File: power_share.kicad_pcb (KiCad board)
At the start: 2 copper layers, 32.5 x 21.1 mm, 22 parts, among them J1 Conn_01x02, J2 Conn_01x03, Q1 NX3008NBKW, Q2 NX3008NBKW, U1 LTC4370

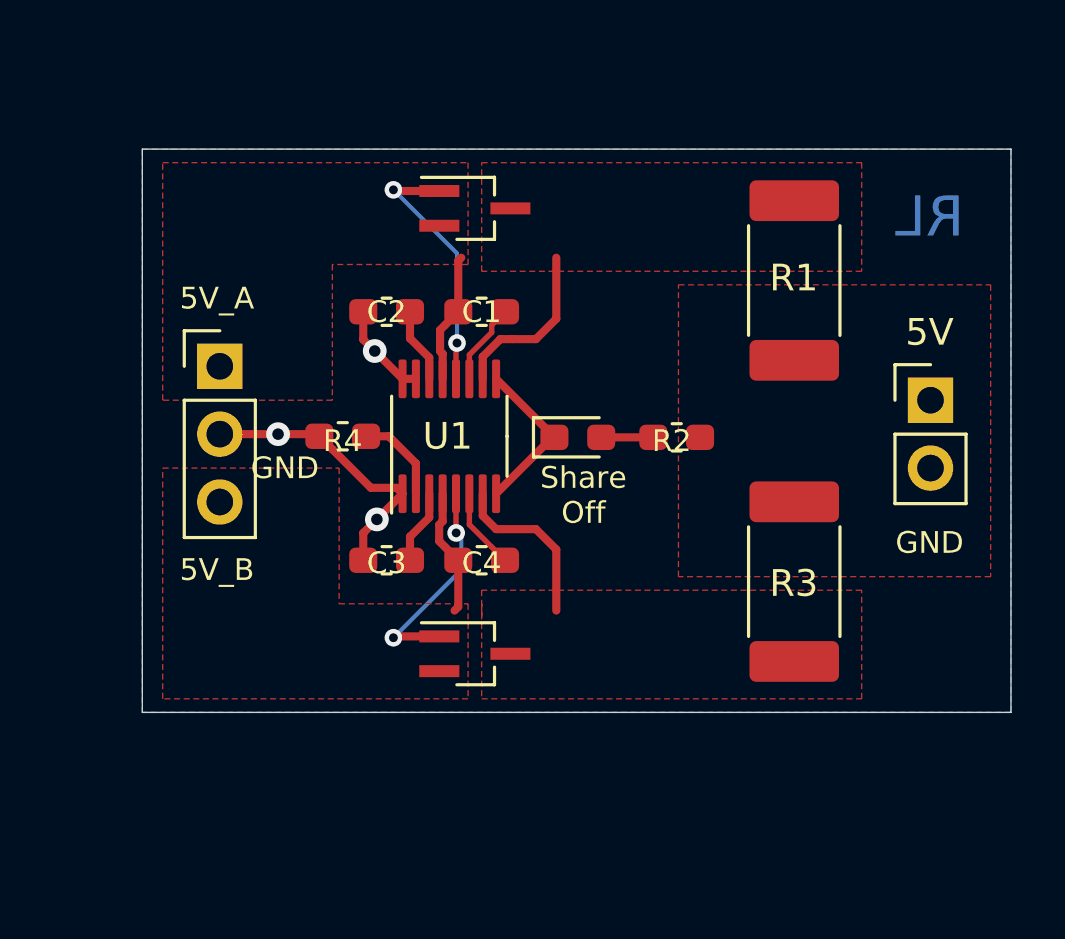
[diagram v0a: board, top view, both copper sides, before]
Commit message: changed to larger mosfet
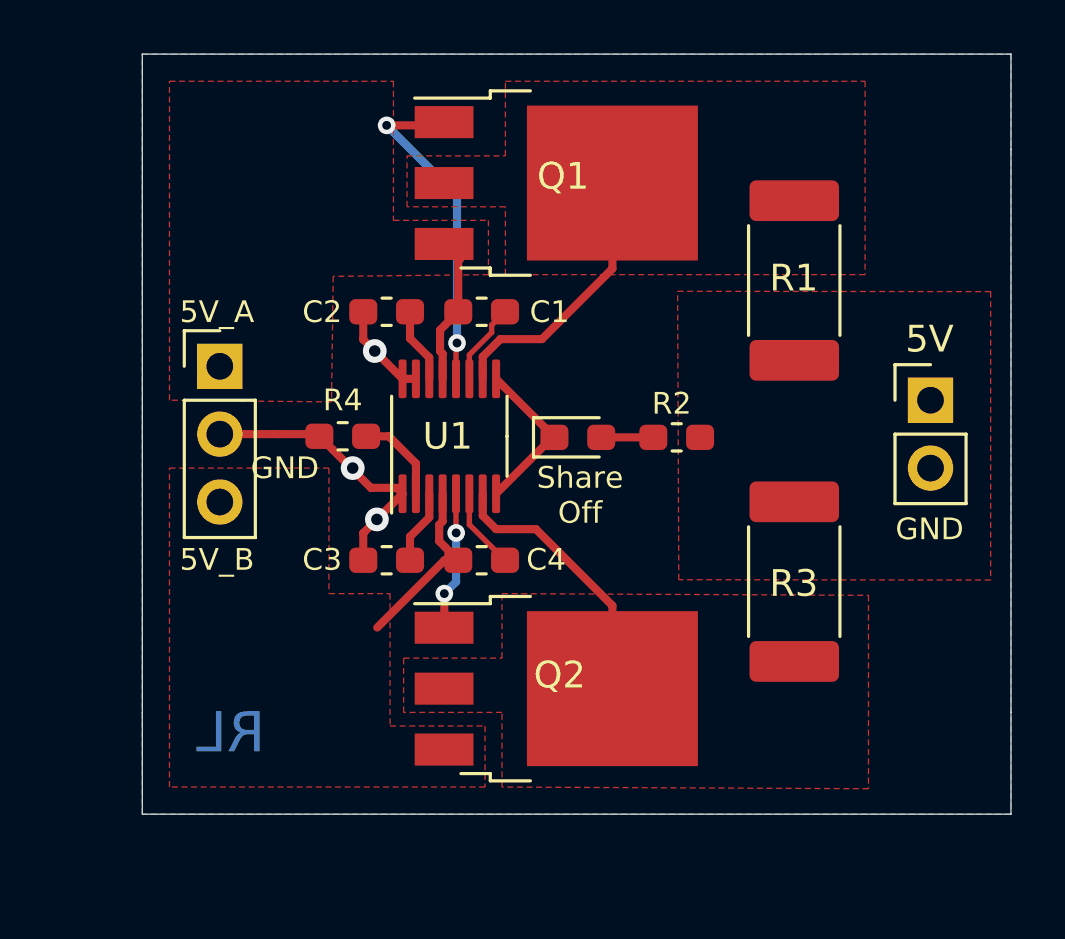
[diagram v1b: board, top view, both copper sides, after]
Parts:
- removed the G*** at (130.6, 93.5)
- removed the G*** at (129.8, 90.2)
- removed the G*** at (125.0, 90.2)
- removed the G*** at (127.3, 88.1)
- removed the G*** at (121.4, 87.4)
- removed the G*** at (129.3, 94.5)
- removed the G*** at (126.7, 92.2)
- removed the G*** at (127.8, 92.5)
- added G***: LOGO, Logos:asian_tiger, F.Cu at (130.6, 94.2)
- Q1, Q2: value NX3008NBKW -> IRLR8726PBF; footprint Package_TO_SOT_SMD:SOT-323_SC-70_Handsoldering -> Package_TO_SOT_SMD:TO-252-3_TabPin4
- moved Q2 3.32 mm to (129.8, 103.5)
- moved Q1 3.19 mm to (129.8, 84.6)
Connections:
- Q1 pad 2: 5V_A -> Net-(Q1-Pad2)
- Q1 pad 3: Net-(Q1-Pad3) -> 5V_A
- Q2 pad 2: 5V_B -> Net-(Q2-Pad2)
- Q2 pad 3: Net-(Q2-Pad3) -> 5V_B
- R1 pad 1: Net-(Q1-Pad3) -> Net-(Q1-Pad2)
- R3 pad 2: Net-(Q2-Pad3) -> Net-(Q2-Pad2)
- U1 pad 10: Net-(Q1-Pad3) -> Net-(Q1-Pad2)
- U1 pad 7: Net-(Q2-Pad3) -> Net-(Q2-Pad2)
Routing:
- net Net-(Q1-Pad2): track 0.00 -> 10.3 mm
- net Net-(Q2-Pad2): track 0.00 -> 10.3 mm
- net Net-(Q1-Pad3): track 6.45 -> 0.00 mm
- net Net-(Q2-Pad3): track 6.39 -> 0.00 mm
- net Net-(Q1-Pad1): track 9.87 -> 12.8 mm
- net Net-(Q2-Pad1): track 8.51 -> 5.64 mm
- net 5V_B: track 4.78 -> 6.92 mm
- added copper zone on F.Cu, net Net-(Q1-Pad2)
- added copper zone on F.Cu, net Net-(Q2-Pad2)
- removed copper zone on F.Cu, net Net-(Q1-Pad3)
- removed copper zone on F.Cu, net Net-(Q2-Pad3)
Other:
- board size 32.5 x 21.1 mm -> 32.5 x 28.4 mm
- board text added: "5V Load Balancer v0.2 © Hyiger Designs 2019"
- board text removed: "Current Balancer v0.1 Hyiger Designs"

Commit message: breadboard friendly. fixed dimensions and traces
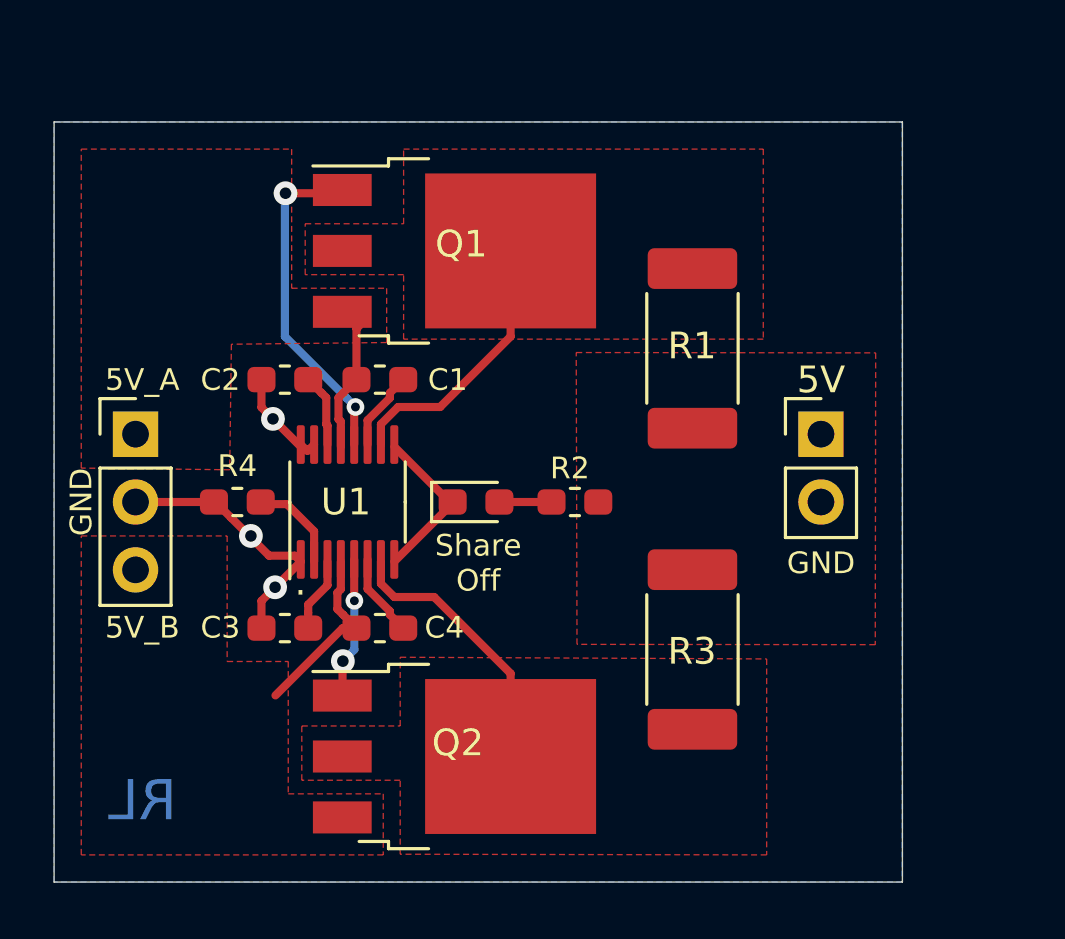
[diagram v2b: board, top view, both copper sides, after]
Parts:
- removed G***: LOGO, Logos:asian_tiger
- moved R4 4.65 mm to (117.9, 96.5)
- moved Q1 4.58 mm to (126.0, 87.1)
- moved Q2 4.58 mm to (126.0, 106.0)
- moved R3 4.58 mm to (134.9, 102.0)
- moved C1 4.58 mm to (123.2, 91.9)
- moved C2 4.58 mm to (119.6, 91.9)
- moved C3 4.58 mm to (119.6, 101.2)
- moved C4 4.58 mm to (123.2, 101.2)
- moved R1 4.58 mm to (134.9, 90.8)
- moved U1 4.54 mm to (122.0, 96.5)
- moved R2 4.51 mm to (130.5, 96.5)
- moved D1 4.51 mm to (126.8, 96.5)
- moved J1 4.29 mm to (139.7, 94.0)
- moved J2 4.05 mm to (114.0, 94.0)
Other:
- board size 32.5 x 28.4 mm -> 31.7 x 28.4 mm
- board text added: "."
- board text added: "5V Load Balancer v0.3 © Hyiger Designs 2019"
- board text removed: "5V Load Balancer v0.2 © Hyiger Designs 2019"

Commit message: final version
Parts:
- added G***: LOGO, Logos:asian_tiger, F.Cu at (126.9, 94.6)
- moved J1 2.54 mm to (139.7, 96.5)
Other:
- board text added: "5V In"
- board text added: "5V Out"
- board text removed: "5V"
- board text removed: "5V_A"
- board text removed: "5V_B"

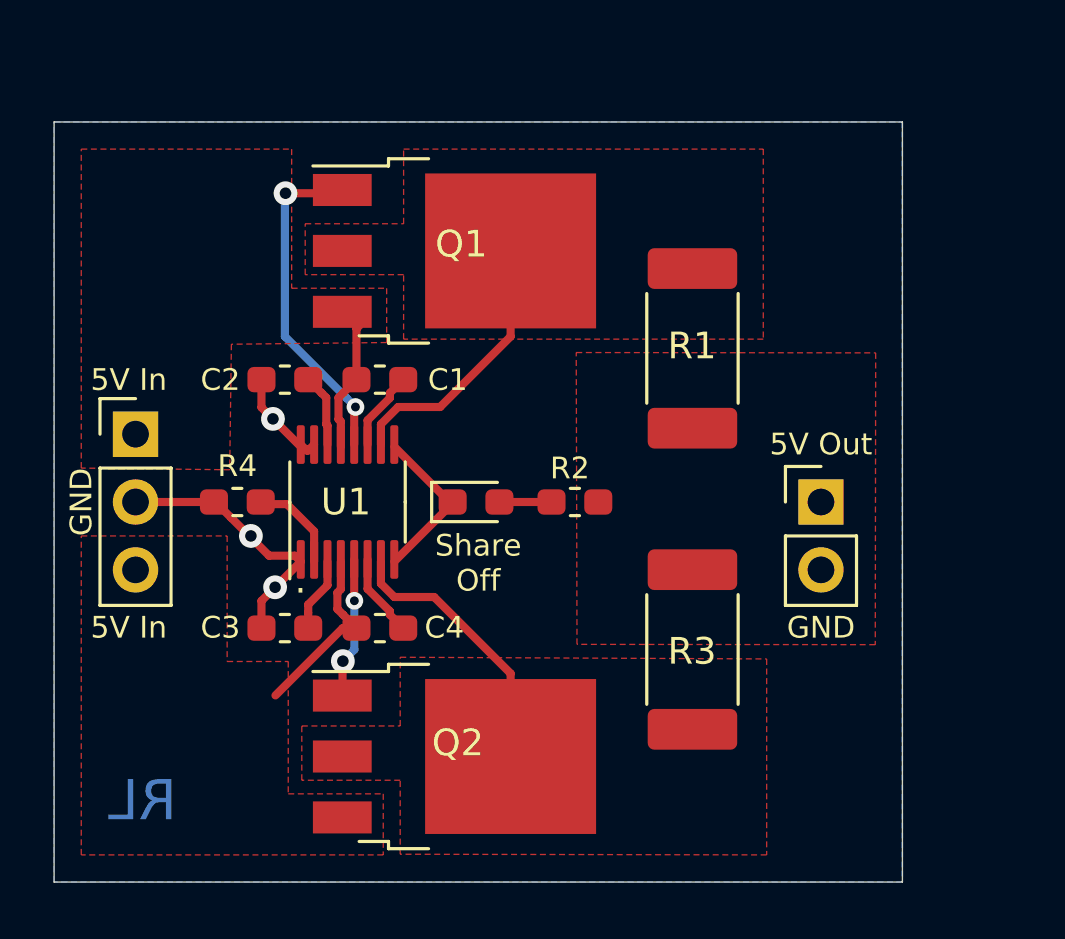
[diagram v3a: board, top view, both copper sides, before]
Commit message: Redesigned layout
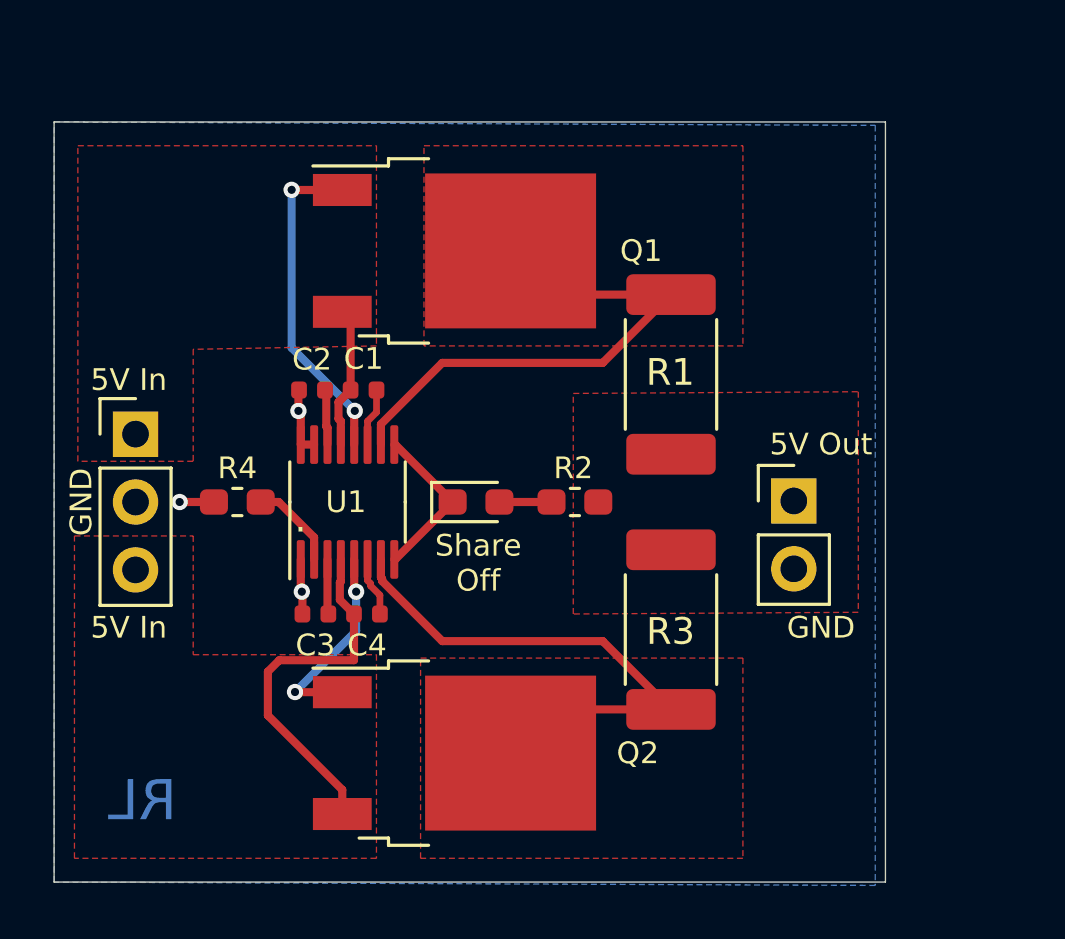
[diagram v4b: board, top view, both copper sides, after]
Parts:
- C1, C4: value 39nF -> 22nF; footprint Capacitor_SMD:C_0603_1608Metric_Pad1.05x0.95mm_HandSolder -> Capacitor_SMD:C_0402_1005Metric
- C2, C3: footprint Capacitor_SMD:C_0603_1608Metric_Pad1.05x0.95mm_HandSolder -> Capacitor_SMD:C_0402_1005Metric
- Q1, Q2: footprint Package_TO_SOT_SMD:TO-252-3_TabPin4 -> Package_TO_SOT_SMD:TO-252-2
- moved R1 1.26 mm to (134.1, 91.7)
- moved C3 1.26 mm to (120.8, 100.7)
- moved R3 1.10 mm to (134.1, 101.3)
- moved C2 1.09 mm to (120.7, 92.3)
- moved J1 1.02 mm to (138.7, 96.5)
- moved G*** 0.76 mm to (126.9, 95.4)
- moved C1 0.72 mm to (122.6, 92.3)
- moved C4 0.72 mm to (122.7, 100.7)
- moved Q2 0.13 mm to (126.0, 105.9)
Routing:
- net Net-(Q1-Pad2): track 10.2 -> 19.6 mm
- net Net-(Q2-Pad2): track 10.3 -> 19.6 mm
- net GND: track 14.7 -> 5.94 mm
- net 5V_B: track 6.92 -> 13.9 mm
- net Net-(Q2-Pad1): track 5.72 -> 7.71 mm
- net Net-(C1-Pad2): track 3.13 -> 2.18 mm
- net Net-(C4-Pad1): track 3.12 -> 2.23 mm
- net Net-(C3-Pad1): track 2.79 -> 2.05 mm
- net Net-(C2-Pad1): track 2.73 -> 2.08 mm
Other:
- board size 31.7 x 28.4 mm -> 31.1 x 28.4 mm
- rule via_min_drill: 0.3302 -> 0.3048
- rule via_min_size: 0.6604 -> 0.6096
- board text added: "5V Load Balancer v0.5 © Hyiger Designs 2019"
- board text removed: "5V Load Balancer v0.3 © Hyiger Designs 2019"

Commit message: layout fixes
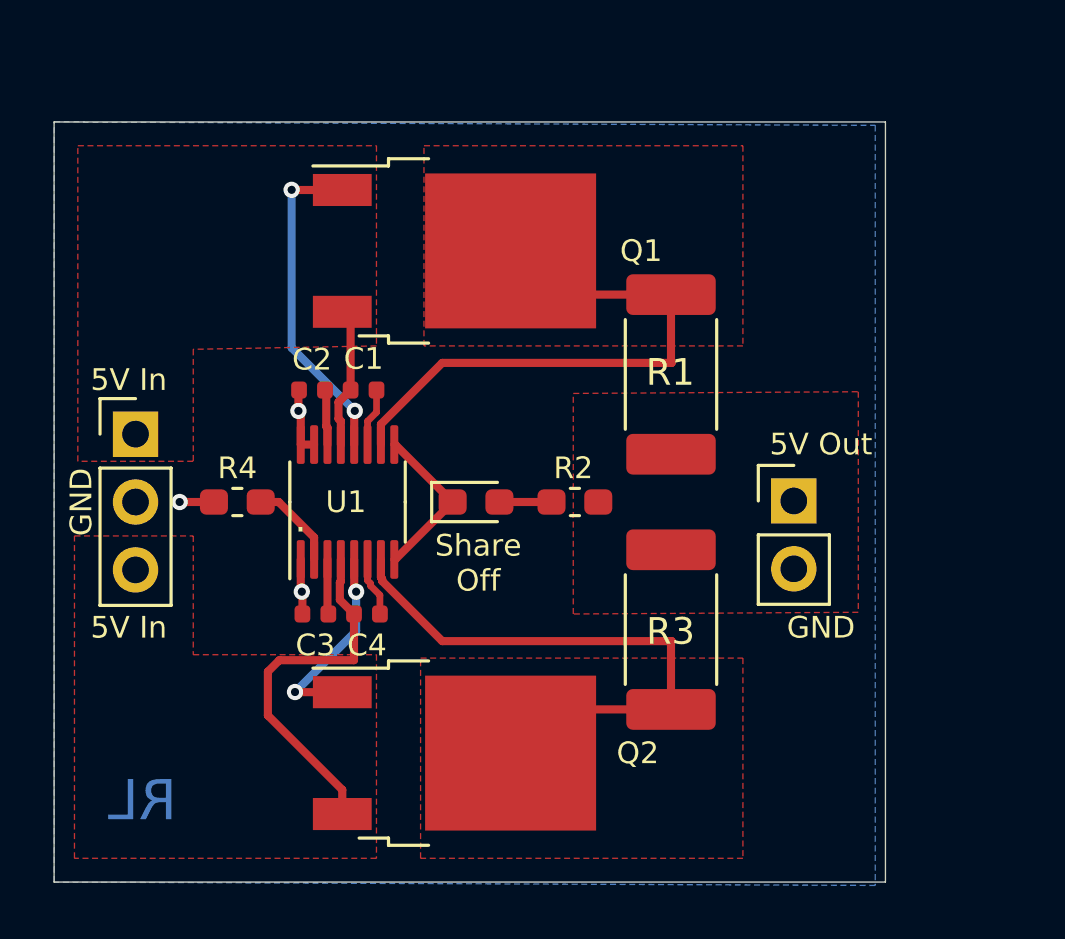
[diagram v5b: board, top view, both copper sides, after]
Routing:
- net Net-(Q2-Pad2): track 19.6 -> 21.2 mm
- net Net-(Q1-Pad2): track 19.6 -> 21.2 mm
